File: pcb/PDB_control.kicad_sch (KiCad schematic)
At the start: 36 parts, among them SW1 SW_Push, SW2 SW_DIP_x02, U12 ATtiny1606-S, U13 MCP2221AxSL

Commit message: Update to KiCAD 9
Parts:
- C21, C23, C24, C25, C26: HTL (none) -> 100128; Vendor HTL -> (none); VendorId 100128 -> (none)
- C22: HTL (none) -> 103620; Vendor HTL -> (none); VendorId 103620 -> (none)
- C27: HTL (none) -> 102538; Vendor HTL -> (none); VendorId 102538 -> (none)
- D10, D11, D9: HTL (none) -> 103607; Vendor HTL -> (none); VendorId 103607 -> (none)
- D12, D13, D14: HTL (none) -> 100193; Vendor HTL -> (none); VendorId 100193 -> (none)
- D6: HTL (none) -> 100206; Vendor HTL -> (none); VendorId 100206 -> (none)
- D7: HTL (none) -> 100458; Vendor HTL -> (none); VendorId 100458 -> (none)
- D8: HTL (none) -> 100459; Vendor HTL -> (none); VendorId 100459 -> (none)
- R27: HTL (none) -> 102967; Vendor HTL -> (none); VendorId 102967 -> (none)
- R28, R30: HTL (none) -> 102951; Vendor HTL -> (none); VendorId 102951 -> (none)
- R29, R36, R37: HTL (none) -> 102944; Vendor HTL -> (none); VendorId 102944 -> (none)
- R31, R33: HTL (none) -> 102973; Vendor HTL -> (none); VendorId 102973 -> (none)
- R32, R35: DigiKey (none) -> RMCF0603ZT0R00CT-ND; Vendor DigiKey -> (none); VendorId RMCF0603ZT0R00CT-ND -> (none)
- R38, R43: HTL (none) -> 102964; Vendor HTL -> (none); VendorId 102964 -> (none)
- R39: HTL (none) -> 102955; Vendor HTL -> (none); VendorId 102955 -> (none)
- R40: HTL (none) -> 102971; Vendor HTL -> (none); VendorId 102971 -> (none)
- R41: HTL (none) -> 102966; Vendor HTL -> (none); VendorId 102966 -> (none)
- R42: HTL (none) -> 102963; Vendor HTL -> (none); VendorId 102963 -> (none)
- SW1: HTL (none) -> 101612; Vendor HTL -> (none); VendorId 101612 -> (none)
- SW2: HTL (none) -> 103604; Vendor HTL -> (none); VendorId 103604 -> (none)
- U12: HTL (none) -> 103450; Vendor HTL -> (none); VendorId 103450 -> (none)
- U13: DigiKey (none) -> 150-MCP2221AT-I/SLCT-ND; Vendor DigiKey -> (none); VendorId 150-MCP2221AT-I/SLCT-ND -> (none)

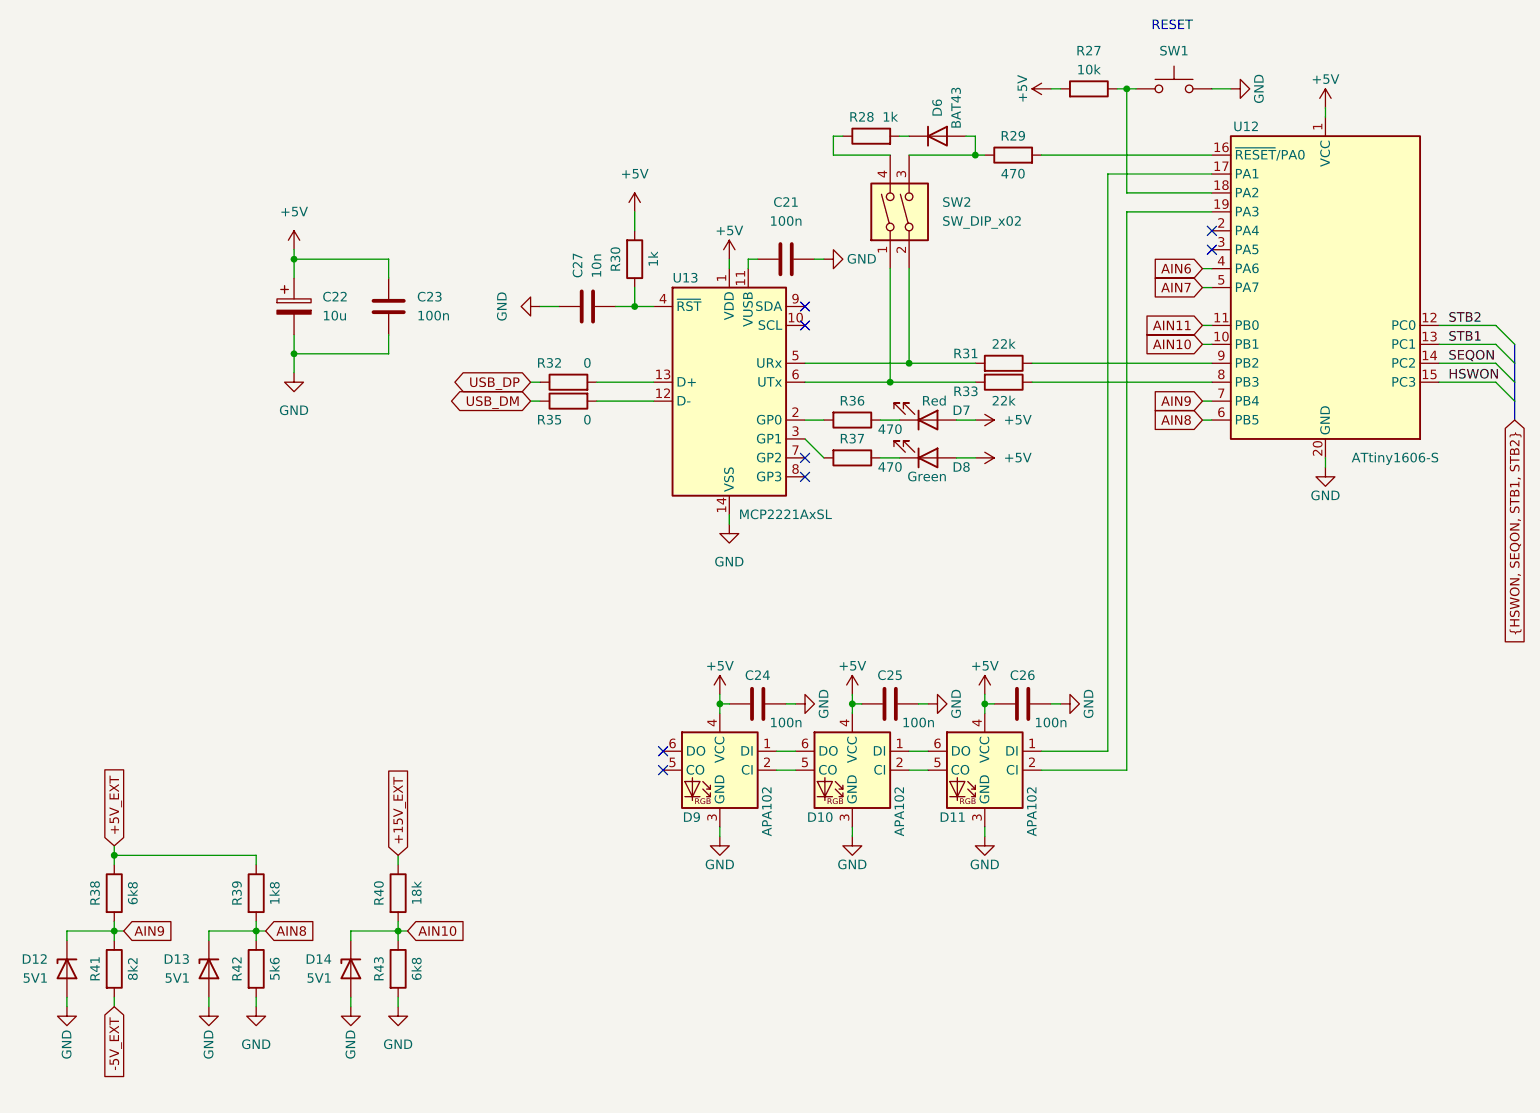
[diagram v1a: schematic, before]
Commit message: Change MCP2221A to FT230X
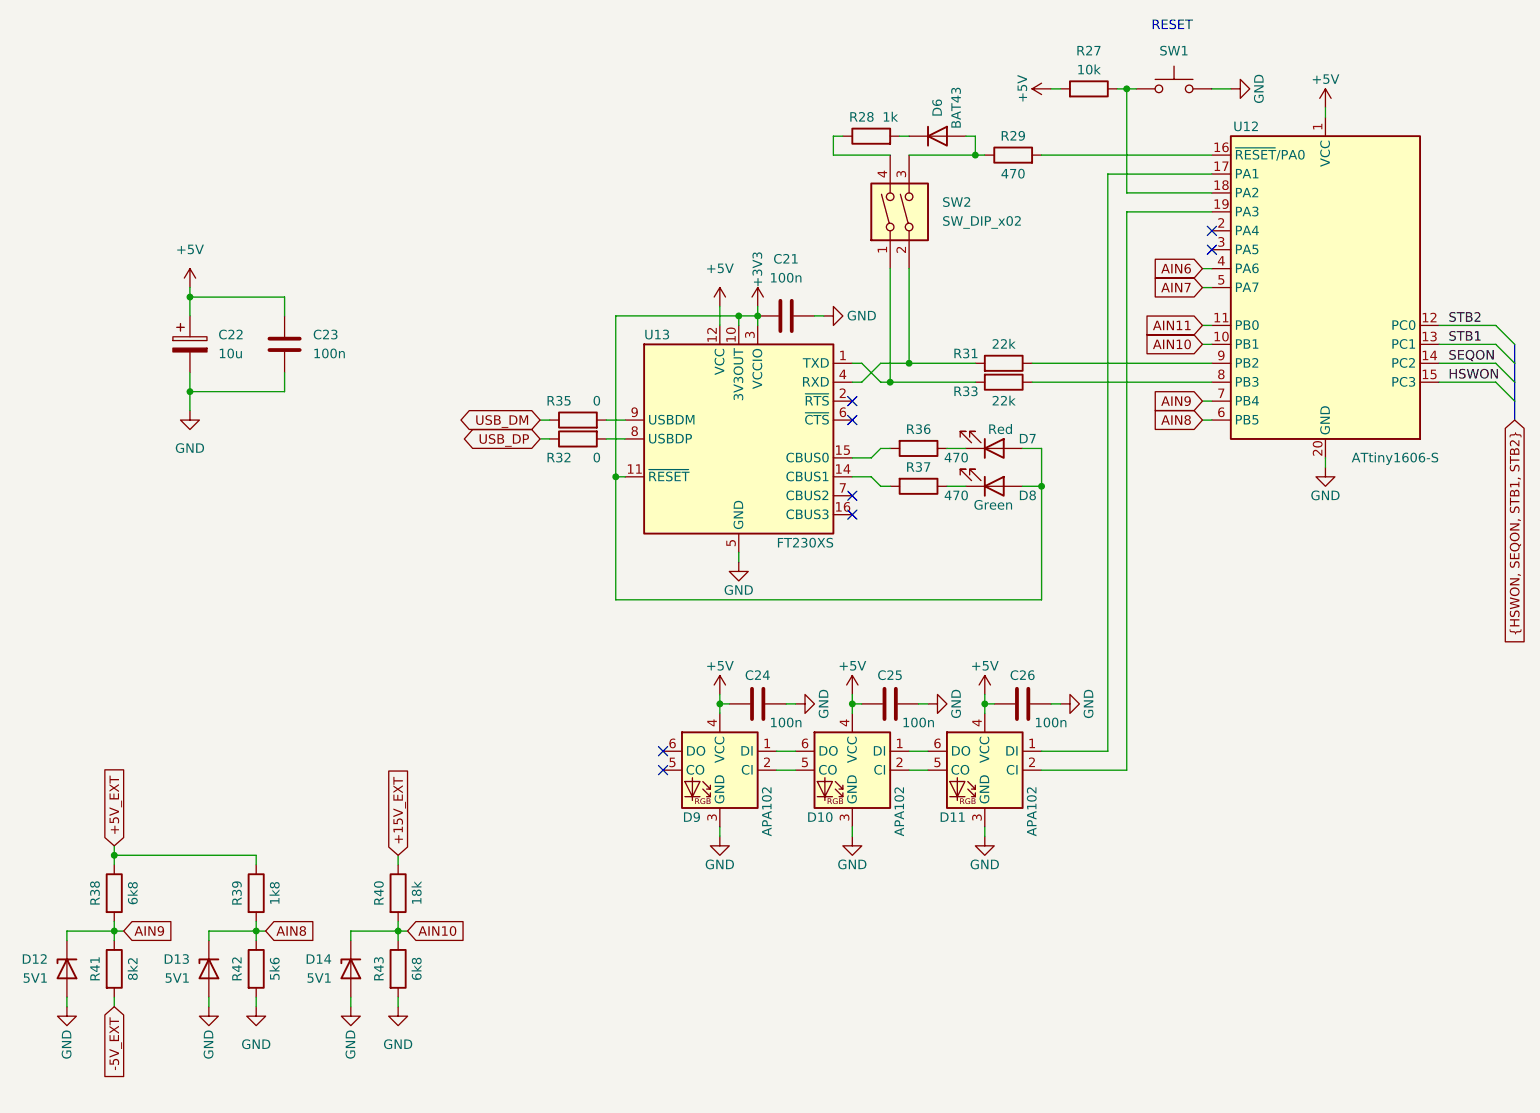
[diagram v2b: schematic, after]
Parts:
- removed C27: 10n, Capacitor_SMD:C_1206_3216Metric, symbol Device:C
- removed R30: 1k, Resistor_SMD:R_1206_3216Metric, symbol Device:R
- removed U13: MCP2221AxSL, Package_SO:SOIC-14_3.9x8.7mm_P1.27mm, symbol Interface_USB:MCP2221AxSL
- added U13: FT230XS, Package_SO:SSOP-16_3.9x4.9mm_P0.635mm, symbol Interface_USB:FT230XS
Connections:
- net +5V: now also U13.12 (VCC); no longer D7.2 (A), D8.2 (A)
- net GND: now also U13.13 (GND), U13.5 (GND)
- net at R33.2, SW2.1: now also U13.1 (TXD)
- net at R31.2, SW2.2: now also U13.4 (RXD)
- net at R32.2: now also U13.8 (USBDP)
- net at R37.2: now also U13.14 (CBUS1)
- net +3V3: now reaches C21.1
- net +3V3: now also D7.2 (A), D8.2 (A), U13.10 (3V3OUT), U13.11 (~{RESET}), U13.3 (VCCIO)
- net at R35.2: now also U13.9 (USBDM)
- net at R36.2: now also U13.15 (CBUS0)
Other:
- moved on the sheet: C22, C23, R32, R35

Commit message: Optimize +3V3 signal
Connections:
- net +3V3: no longer names the net of C21.1, D7.2 (A), D8.2 (A), U13.10 (3V3OUT), U13.11 (~{RESET}), U13.3 (VCCIO)
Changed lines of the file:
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@@
 	(wire
 		(pts
-			(xy 128.27 72.39) (xy 128.27 73.66)
-		)
-		(stroke
-			(width 0)
-			(type default)
-		)
-	)
-	(wire
-		(pts
 			(xy 187.96 67.31) (xy 189.23 67.31)
 		)
@@
 					(unit 1)
 				)
-			)
-		)
-	)
-	(symbol
-		(lib_id "power:+3V3")
-		(at 128.27 72.39 0)
-		(unit 1)
-		(exclude_from_sim no)
-		(in_bom yes)
-		(on_board yes)
-		(dnp no)
-		(property "Reference" "#PWR082"
-			(at 128.27 76.2 0)
-			(effects
-				(font
-					(size 1.27 1.27)
-				)
-				(hide yes)
-			)
-		)
-		(property "Value" "+3V3"
-			(at 128.27 69.85 90)
-			(effects
-				(font
-					(size 1.27 1.27)
-				)
-				(justify left)
-			)
-		)
-		(property "Footprint" ""
-			(at 128.27 72.39 0)
-			(effects
-				(font
-					(size 1.27 1.27)
-				)
-				(hide yes)
-			)
-		)
-		(property "Datasheet" ""
-			(at 128.27 72.39 0)
-			(effects
-				(font
-					(size 1.27 1.27)
-				)
-				(hide yes)
-			)
-		)
-		(property "Description" "Power symbol creates a global label with name \"+3V3\""
-			(at 128.27 72.39 0)
-			(effects
-				(font
-					(size 1.27 1.27)
-				)
-				(hide yes)
-			)
-		)
-		(pin "1"
-		)
-		(instances
-			(project "PDB"
-				(path "/9334361a-f7a5-4302-90e9-4b89798c8fc6/589f6121-3290-4060-8c95-f630f62d2a0d"
-					(reference "#PWR082")
-					(unit 1)
-				)
